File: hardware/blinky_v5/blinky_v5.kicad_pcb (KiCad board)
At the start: 2 copper layers, 130 x 70 mm, 235 parts, among them J1 RJ45, J10 Conn_01x04, J11 Conn_01x08, J12 Conn_01x06, J2 Conn_01x06_Pin, J3 Conn_01x05_Pin, J5 Conn_01x06_Pin, J6 Conn_01x04_Pin, J7 Conn_01x04_Pin, J8 Conn_01x02, J9 Conn_02x10_Odd_Even, Q1 2N7002, Q2 2N7002, Q3 2N7002, Q4 2N7002, Q5 2N7002, Q6 2N7002, Q7 2N7002, Q8 2N7002, U1 ADA4807-1, U10 STM32F405RGTx, U11 AMS1117-3.3, U12 BA50DD0WHFP-TR, U13 M24C02-RMN, U2 SN74LVC1G14DBV, U3 SN74LVC1G14DBV, U4 ADA4807-1, U5 ADA4807-1, U6 TLV3603DCKR, U7 SN74LVC1G14DBV, U8 TLV3603DCKR, U9 L78L05_SOT89, X1 GTXO-14V (2.048MHz), X2 GTXO-14V (2.048MHz), Y1 AOCJY4A-10.000MHZ-SW, Y2 16MHz

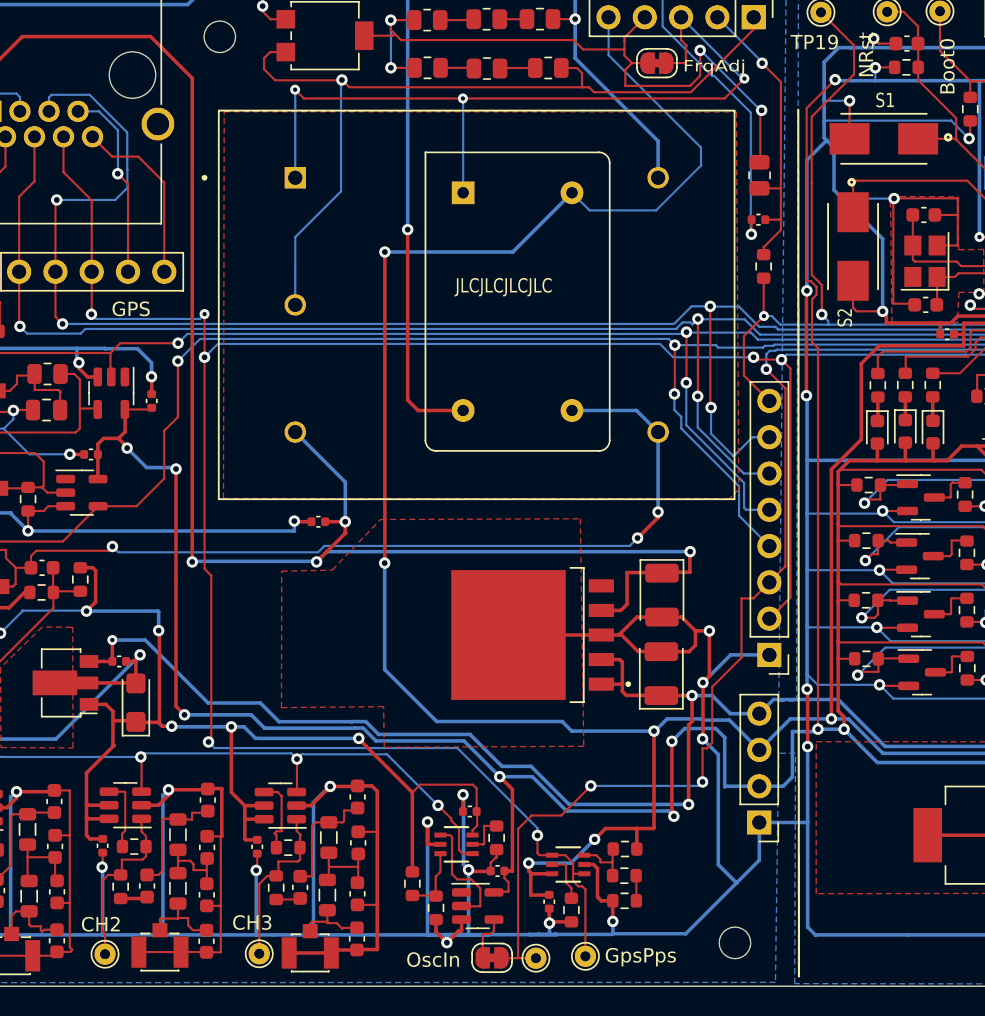
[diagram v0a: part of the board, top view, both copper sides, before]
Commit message: fix GPS PPS routing bug
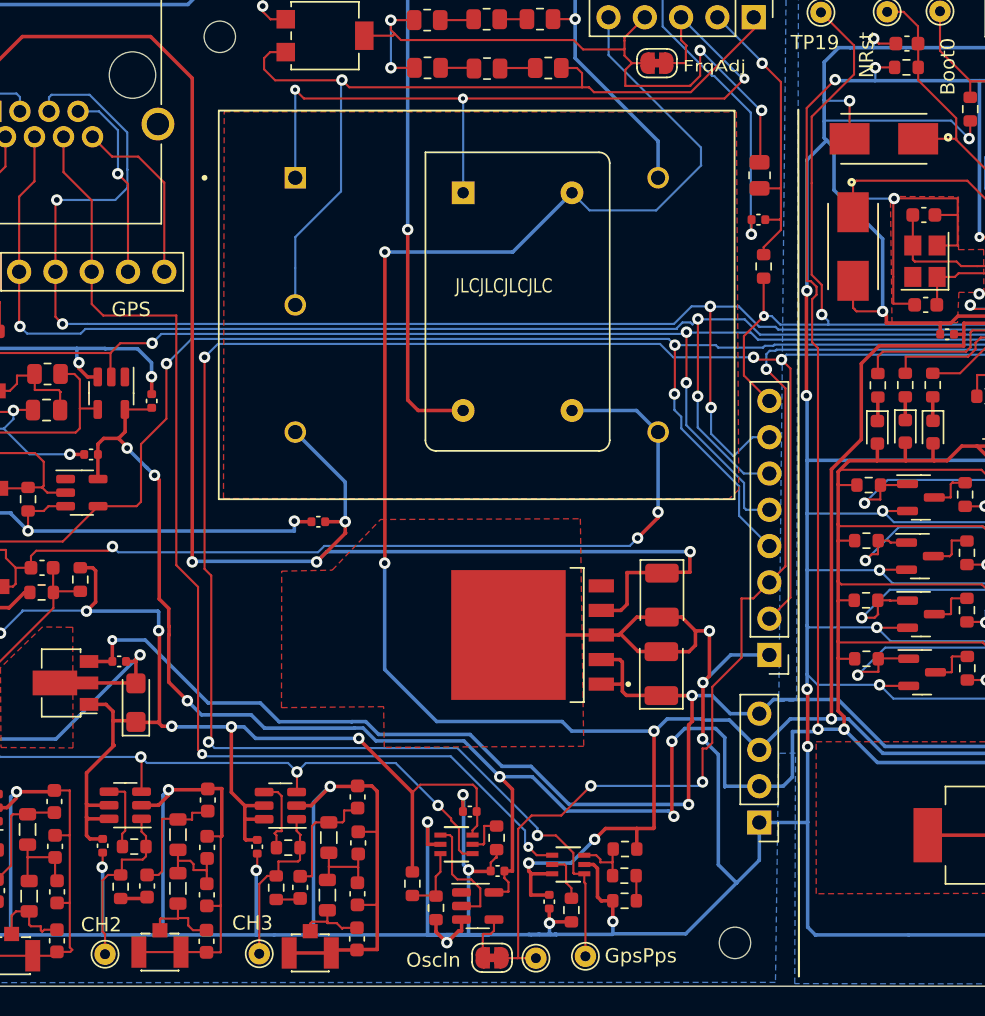
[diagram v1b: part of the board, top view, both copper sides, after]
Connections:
- J1 pad 6: GPS_PPS -> /GPS_EXT_PPS
- J2 pad 4: GPS_PPS -> /GPS_EXT_PPS
- U8 pad 4: GPS_PPS -> /GPS_EXT_PPS
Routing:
- net /GPS_EXT_PPS: track 0.00 -> 78.2 mm, vias 0 -> 2
- net GPS_PPS: track 177.9 -> 152.6 mm, vias 8 -> 6
- net +3.3V: track 470.5 -> 468.5 mm
- net /10Mhz2.5V: track 66.7 -> 65.8 mm

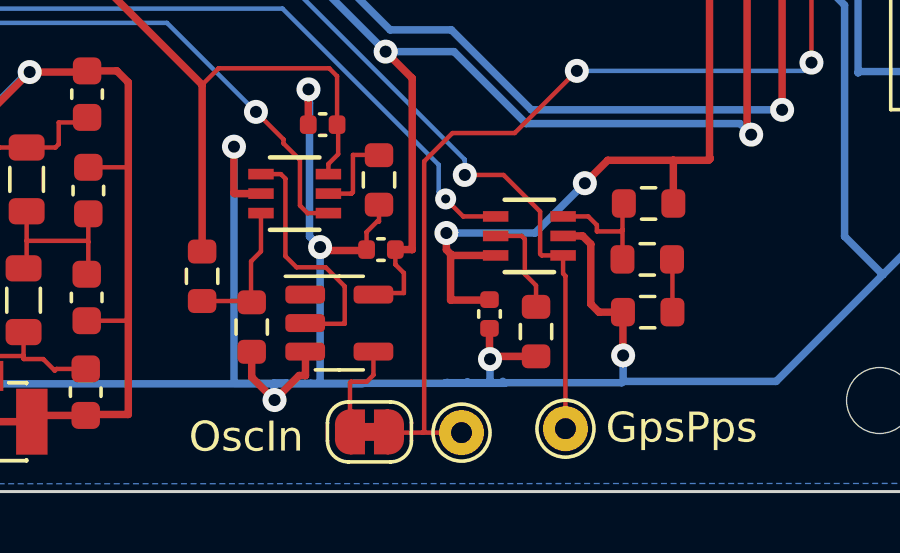
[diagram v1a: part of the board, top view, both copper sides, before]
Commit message: filter power splits
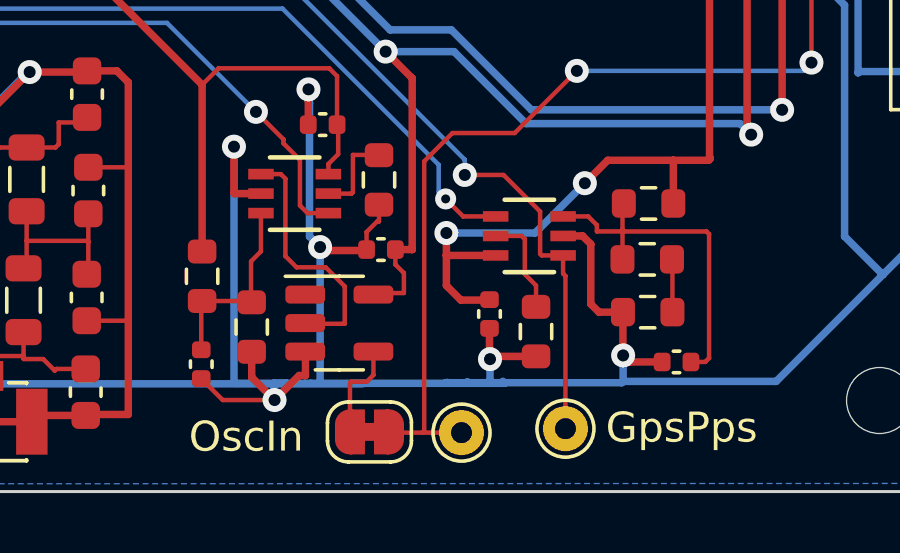
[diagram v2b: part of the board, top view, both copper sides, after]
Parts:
- added C48: 100nF, Capacitor_SMD:C_0402_1005Metric, F.Cu at (151.9, 115.7)
- added C49: 100nF, Capacitor_SMD:C_0402_1005Metric, F.Cu at (136.1, 115.8)
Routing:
- net Net-(U8-IN+): track 4.21 -> 11.9 mm
- net GND: track 1171.7 -> 1175.8 mm
- net Net-(U6-IN+): track 4.79 -> 6.43 mm

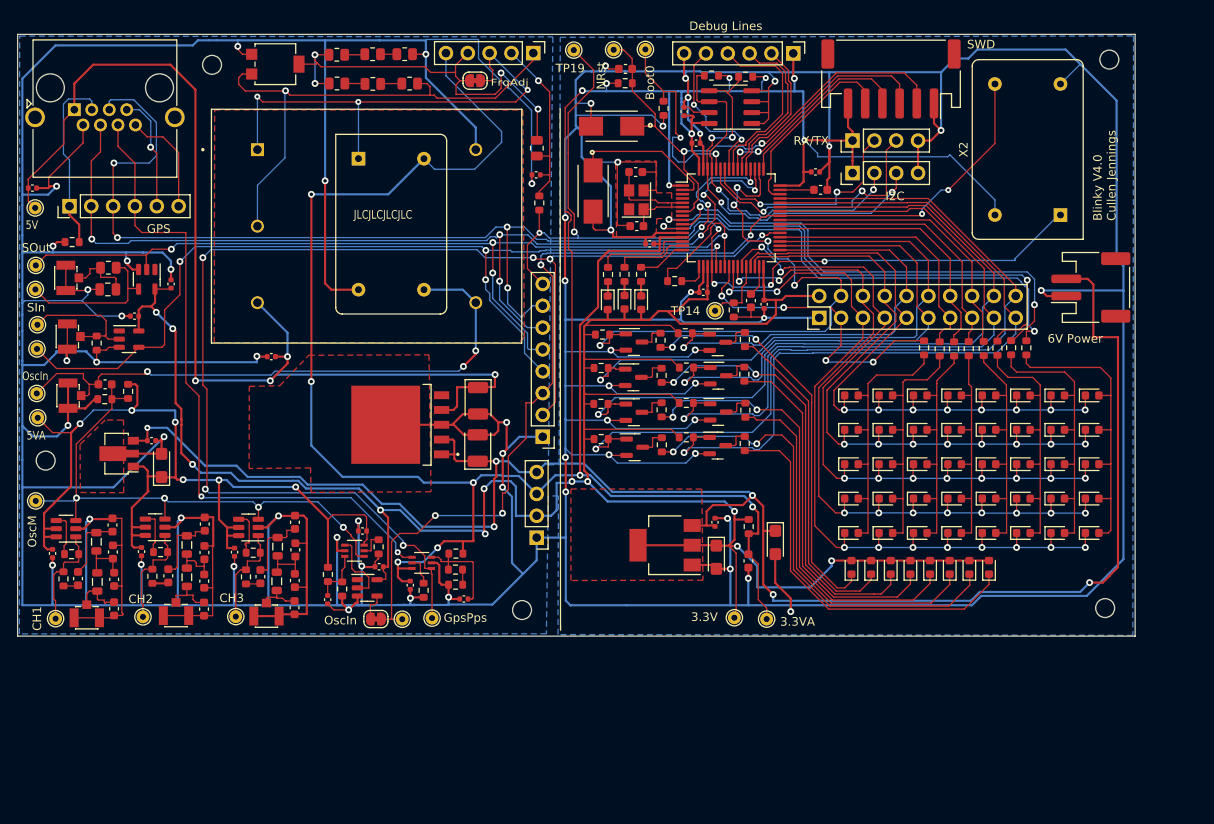
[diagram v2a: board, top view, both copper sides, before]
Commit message: put the serial ouput on connector
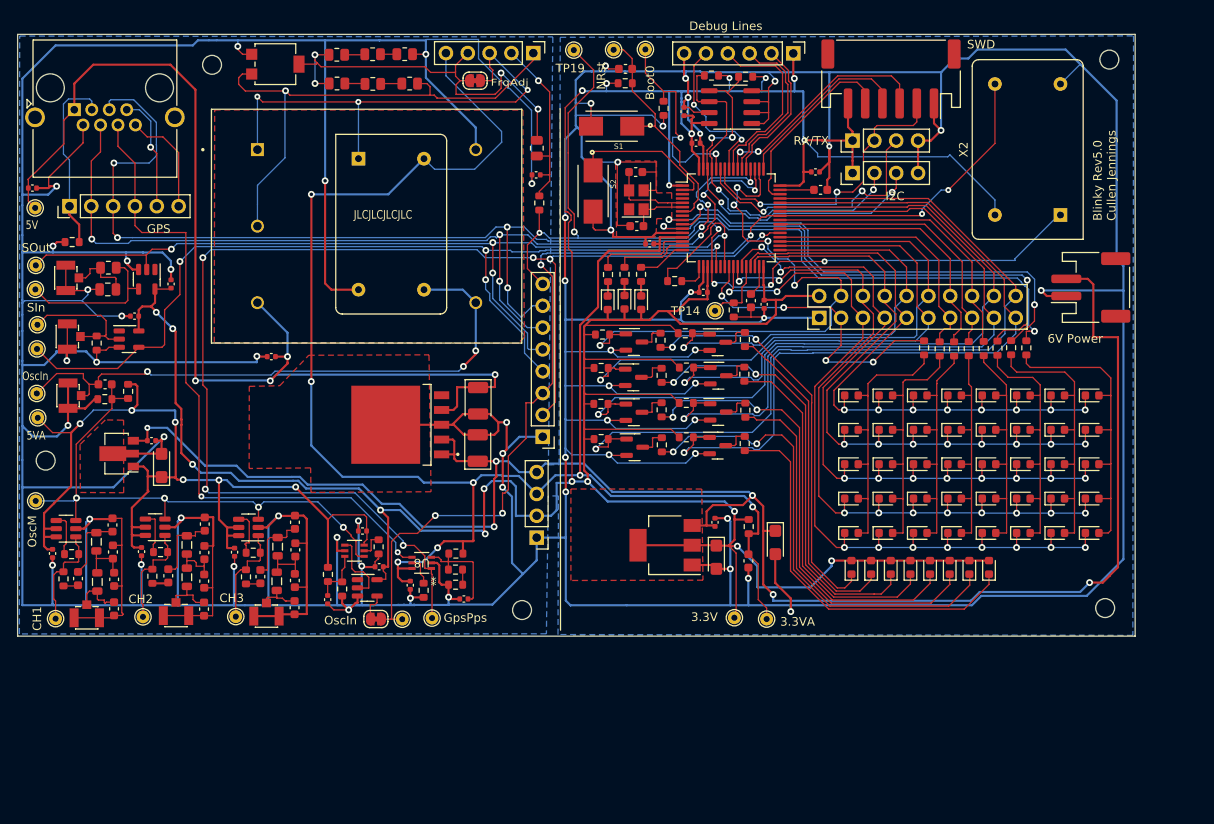
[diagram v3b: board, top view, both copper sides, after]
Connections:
- J12 pad 2: /NRST -> /USB_RX
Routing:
- net /NRST: track 61.6 -> 27.5 mm, vias 2 -> 0
- net /USB_RX: track 26.0 -> 34.8 mm
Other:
- board text added: "Blinky Rev5.0 Cullen Jennings"
- board text removed: "Blinky V4.0 Cullen Jennings"
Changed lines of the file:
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@@
       (net 26 "GND") (pinfunction "Pin_1") (pintype "passive"))
     (pad "2" smd roundrect (at -3 -2.85 180) (size 1 3.5) (layers "F.Cu" "F.Paste" "F.Mask") (roundrect_rratio 0.25)
-      (net 52 "/NRST") (pinfunction "Pin_2") (pintype "passive"))
+      (net 41 "/USB_RX") (pinfunction "Pin_2") (pintype "passive"))
     (pad "3" smd roundrect (at -1 -2.85 180) (size 1 3.5) (layers "F.Cu" "F.Paste" "F.Mask") (roundrect_rratio 0.25)
       (net 44 "/SWDTRC") (pinfunction "Pin_3") (pintype "passive"))
@@
     (property "Sheetname" "")
     (attr smd)
-    (fp_text reference "S1" (at -0.818505 -2.357851 180) (layer "F.SilkS") hide
+    (fp_text reference "S1" (at -0.818505 -2.357851 180) (layer "F.SilkS")
         (effects (font (size 0.640395 0.640395) (thickness 0.15)))
     )
@@
     (property "Sheetname" "")
     (attr smd)
-    (fp_text reference "S2" (at -0.818505 -2.357851 -90) (layer "F.SilkS") hide
+    (fp_text reference "S2" (at -0.818505 -2.357851 -90) (layer "F.SilkS")
         (effects (font (size 0.640395 0.640395) (thickness 0.15)))
     )
@@
     (property "ki_keywords" "TLV3603DCKR")
     (attr smd)
-    (fp_text reference "U8" (at 0 0 180 unlocked) (layer "F.SilkS") hide
+    (fp_text reference "U8" (at 0 0 180 unlocked) (layer "F.SilkS")
         (effects (font (size 1 1) (thickness 0.15)))
     )
@@
         (effects (font (size 1 1) (thickness 0.15)))
     )
-    (fp_text user "*" (at -0.3175 -1.0033 180 unlocked) (layer "F.Fab")
+    (fp_text user "*" (at -1.37795 -2.1486 180) (layer "F.SilkS")
         (effects (font (size 1 1) (thickness 0.15)))
     )
-    (fp_text user "${REFERENCE}" (at 0 0 180 unlocked) (layer "F.Fab")
+    (fp_text user "*" (at -1.37795 -2.1486 180 unlocked) (layer "F.SilkS")
         (effects (font (size 1 1) (thickness 0.15)))
     )
@@
         (effects (font (size 1 1) (thickness 0.15)))
     )
+    (fp_text user "*" (at -0.3175 -1.0033 180 unlocked) (layer "F.Fab")
+        (effects (font (size 1 1) (thickness 0.15)))
+    )
+    (fp_text user "${REFERENCE}" (at 0 0 180 unlocked) (layer "F.Fab")
+        (effects (font (size 1 1) (thickness 0.15)))
+    )
     (fp_line (start -0.8255 1.2065) (end 0.8255 1.2065)
       (stroke (width 0.1524) (type solid)) (layer "F.SilkS"))
@@
   (gr_line (start 100 50) (end 100 120)
     (stroke (width 0.1) (type default)) (layer "Edge.Cuts"))
-  (gr_text "Blinky V4.0	\nCullen Jennings" (at 227.841995 71.695224 90) (layer "F.SilkS")
+  (gr_text "Blinky Rev5.0	\nCullen Jennings" (at 227.841995 71.695224 90) (layer "F.SilkS")
     (effects (font (size 1 1) (thickness 0.15)) (justify left bottom))
   )
@@
   (segment (start 204.315382 85.266846) (end 204.589437 84.992791) (width 0.15) (layer "B.Cu") (net 40))
   (segment (start 170.14172 87.869336) (end 185.333238 87.869336) (width 0.15) (layer "B.Cu") (net 40))
+  (segment (start 199.665058 60.915886) (end 199.665058 62.352698) (width 0.15) (layer "F.Cu") (net 41))
+  (segment (start 204.600617 60.190807) (end 204.187406 60.604018) (width 0.15) (layer "F.Cu") (net 41))
   (segment (start 184.093152 69.158513) (end 185.792931 69.158513) (width 0.15) (layer "F.Cu") (net 41))
+  (segment (start 204.187406 60.604018) (end 199.976926 60.604018) (width 0.15) (layer "F.Cu") (net 41))
   (segment (start 198.395361 67.108453) (end 198.395361 63.622395) (width 0.15) (layer "F.Cu") (net 41))
   (segment (start 197.161704 68.34211) (end 198.395361 67.108453) (width 0.15) (layer "F.Cu") (net 41))
+  (segment (start 204.600617 58.033527) (end 204.600617 60.190807) (width 0.15) (layer "F.Cu") (net 41))
   (segment (start 182.265261 65.666385) (end 182.265261 67.330622) (width 0.15) (layer "F.Cu") (net 41))
   (segment (start 182.265261 67.330622) (end 184.093152 69.158513) (width 0.15) (layer "F.Cu") (net 41))
@@
   (segment (start 185.792931 69.158513) (end 186.400963 69.766545) (width 0.15) (layer "F.Cu") (net 41))
   (segment (start 195.317338 68.34211) (end 197.161704 68.34211) (width 0.15) (layer "F.Cu") (net 41))
+  (segment (start 199.976926 60.604018) (end 199.665058 60.915886) (width 0.15) (layer "F.Cu") (net 41))
   (via (at 186.400963 69.766545) (size 0.7) (drill 0.3) (layers "F.Cu" "B.Cu") (net 41))
   (via (at 195.317338 68.34211) (size 0.8) (drill 0.4) (layers "F.Cu" "B.Cu") (net 41))
@@
   (segment (start 173.909891 84.724686) (end 173.943306 84.758101) (width 0.15) (layer "F.Cu") (net 51))
   (segment (start 172.629756 85.786118) (end 173.780088 85.786118) (width 0.15) (layer "F.Cu") (net 51))
-  (segment (start 204.600617 55.933323) (end 204.600617 58.033527) (width 0.15) (layer "F.Cu") (net 52))
-  (segment (start 179.171005 69.214541) (end 178.697991 69.687555) (width 0.15) (layer "F.Cu") (net 52))
-  (segment (start 177.027065 63.60858) (end 177.527097 63.60858) (width 0.15) (layer "F.Cu") (net 52))
-  (segment (start 178.697991 69.687555) (end 178.697991 70.162975) (width 0.15) (layer "F.Cu") (net 52))
-  (segment (start 177.527097 63.60858) (end 177.527097 65.705073) (width 0.15) (layer "F.Cu") (net 52))
-  (segment (start 178.697991 70.162975) (end 178.269581 70.591385) (width 0.15) (layer "F.Cu") (net 52))
+  (segment (start 177.027065 63.60858) (end 177.027065 65.205041) (width 0.15) (layer "F.Cu") (net 52))
+  (segment (start 174.163497 60.660997) (end 174.163497 60.745012) (width 0.15) (layer "F.Cu") (net 52))
   (segment (start 170.477335 51.793873) (end 171.489945 52.806483) (width 0.15) (layer "F.Cu") (net 52))
-  (segment (start 174.163497 60.745012) (end 177.027065 63.60858) (width 0.15) (layer "F.Cu") (net 52))
   (segment (start 169.331579 51.793873) (end 170.477335 51.793873) (width 0.15) (layer "F.Cu") (net 52))
-  (segment (start 203.147243 54.479949) (end 204.600617 55.933323) (width 0.15) (layer "F.Cu") (net 52))
-  (segment (start 174.145183 60.679311) (end 174.163497 60.660997) (width 0.15) (layer "F.Cu") (net 52))
-  (segment (start 187.04519 62.683637) (end 195.248878 54.479949) (width 0.15) (layer "F.Cu") (net 52))
-  (segment (start 177.527097 65.705073) (end 179.171005 67.348981) (width 0.15) (layer "F.Cu") (net 52))
   (segment (start 178.269581 70.591385) (end 177.340261 70.591385) (width 0.15) (layer "F.Cu") (net 52))
+  (segment (start 174.145183 60.679311) (end 174.163497 60.660997) (width 0.15) (layer "F.Cu") (net 52))
+  (segment (start 178.697991 69.687555) (end 178.697991 70.162975) (width 0.15) (layer "F.Cu") (net 52))
+  (segment (start 179.171005 69.214541) (end 178.697991 69.687555) (width 0.15) (layer "F.Cu") (net 52))
+  (segment (start 179.171005 67.348981) (end 179.171005 69.214541) (width 0.15) (layer "F.Cu") (net 52))
   (segment (start 171.504967 55.681887) (end 171.504967 54.03133) (width 0.15) (layer "F.Cu") (net 52))
   (segment (start 171.489945 52.806483) (end 171.489945 54.016308) (width 0.15) (layer "F.Cu") (net 52))
   (segment (start 171.500558 60.679311) (end 174.145183 60.679311) (width 0.15) (layer "F.Cu") (net 52))
-  (segment (start 195.248878 54.479949) (end 203.147243 54.479949) (width 0.15) (layer "F.Cu") (net 52))
+  (segment (start 178.697991 70.162975) (end 178.269581 70.591385) (width 0.15) (layer "F.Cu") (net 52))
+  (segment (start 177.027065 65.205041) (end 179.171005 67.348981) (width 0.15) (layer "F.Cu") (net 52))
   (segment (start 174.163497 59.238532) (end 174.163497 60.660997) (width 0.15) (layer "F.Cu") (net 52))
-  (segment (start 179.171005 67.348981) (end 179.171005 69.214541) (width 0.15) (layer "F.Cu") (net 52))
   (segment (start 171.504967 56.580002) (end 174.163497 59.238532) (width 0.15) (layer "F.Cu") (net 52))
-  (segment (start 174.163497 60.660997) (end 174.163497 60.745012) (width 0.15) (layer "F.Cu") (net 52))
+  (segment (start 174.163497 60.745012) (end 177.027065 63.60858) (width 0.15) (layer "F.Cu") (net 52))
   (segment (start 171.504967 54.03133) (end 171.489945 54.016308) (width 0.15) (layer "F.Cu") (net 52))
   (segment (start 171.504967 55.681887) (end 171.504967 56.580002) (width 0.15) (layer "F.Cu") (net 52))
-  (segment (start 186.586277 62.683637) (end 187.04519 62.683637) (width 0.15) (layer "F.Cu") (net 52))
-  (via (at 177.527097 63.60858) (size 0.8) (drill 0.4) (layers "F.Cu" "B.Cu") (net 52))
-  (via (at 186.586277 62.683637) (size 0.8) (drill 0.4) (layers "F.Cu" "B.Cu") (net 52))
-  (segment (start 177.589495 63.546182) (end 177.527097 63.60858) (width 0.15) (layer "B.Cu") (net 52))
-  (segment (start 185.494758 63.327994) (end 184.660927 63.327994) (width 0.15) (layer "B.Cu") (net 52))
-  (segment (start 180.629097 63.546182) (end 177.589495 63.546182) (width 0.15) (layer "B.Cu") (net 52))
-  (segment (start 186.586277 62.683637) (end 186.323547 62.946367) (width 0.15) (layer "B.Cu") (net 52))
-  (segment (start 186.323547 62.946367) (end 185.876385 62.946367) (width 0.15) (layer "B.Cu") (net 52))
-  (segment (start 184.335927 63.002994) (end 181.172285 63.002994) (width 0.15) (layer "B.Cu") (net 52))
-  (segment (start 184.660927 63.327994) (end 184.335927 63.002994) (width 0.15) (layer "B.Cu") (net 52))
-  (segment (start 185.876385 62.946367) (end 185.494758 63.327994) (width 0.15) (layer "B.Cu") (net 52))
-  (segment (start 181.172285 63.002994) (end 180.629097 63.546182) (width 0.15) (layer "B.Cu") (net 52))
   (segment (start 175.146386 56.647349) (end 175.146386 56.634486) (width 0.15) (layer "F.Cu") (net 53))
   (segment (start 175.146386 56.634486) (end 173.029499 54.517599) (width 0.15) (layer "F.Cu") (net 53))
